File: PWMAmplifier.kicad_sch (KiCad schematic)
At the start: 13 parts, among them Q27 2N7000, Q28 2N7000, Q29 2N7000, Q30 2N7000, Q31 2N7000, Q32 2N7000

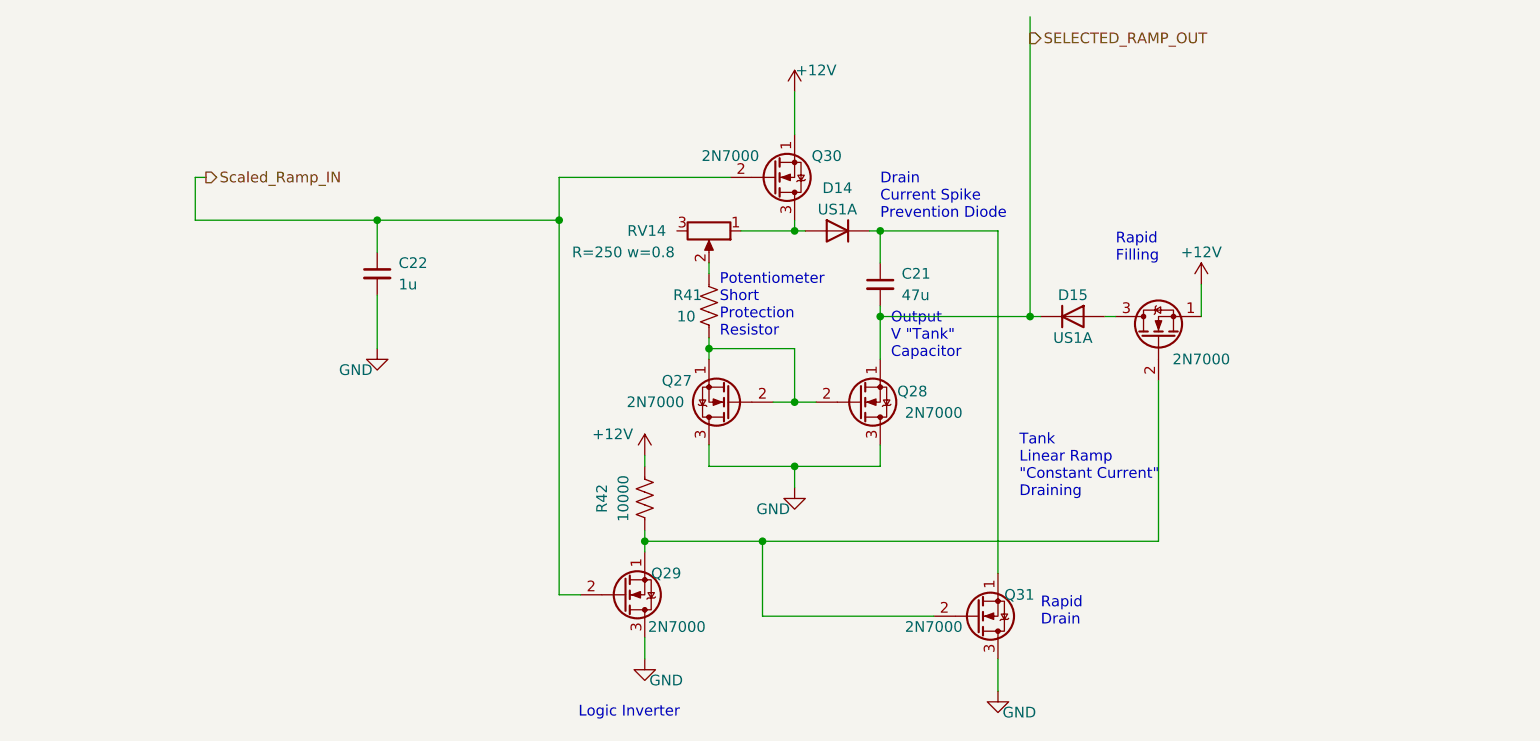
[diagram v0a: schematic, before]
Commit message: added new spice directives to improve simulation speed, added sections for motor drivers, micro controlers, i2c bus connections, realized that focusing coils, hv, horizontal and vertical ramp will need time stable signals (not voltage dependant like with a voltage controlled oscilator) so it will be much simpler to design them with micro controllers
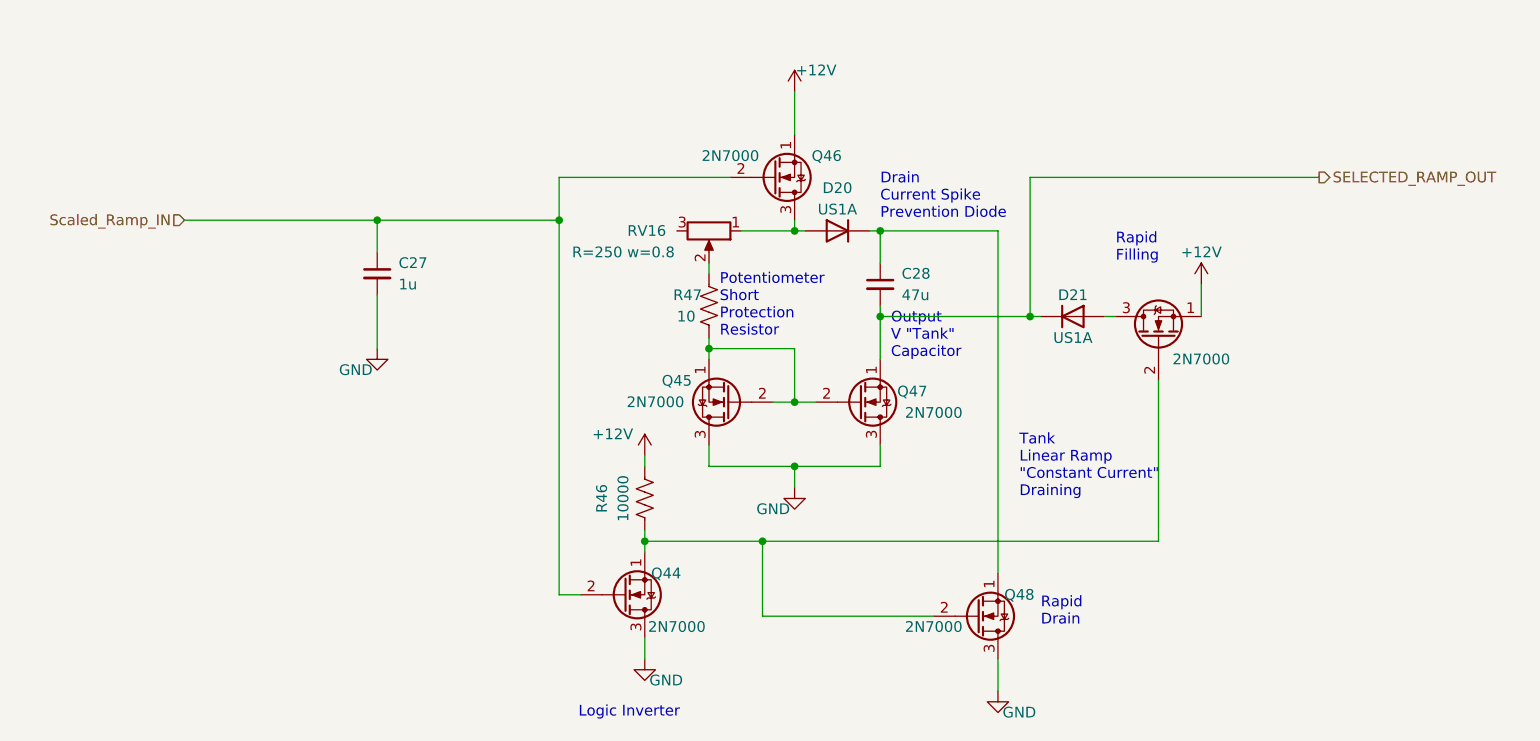
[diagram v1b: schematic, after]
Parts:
- renumbered C22 to C27, C21 to C28, D14 to D20, D15 to D21, Q29 to Q44, Q27 to Q45, Q30 to Q46, Q28 to Q47, Q31 to Q48, Q32 to Q49, R42 to R46, R41 to R47, RV14 to RV16
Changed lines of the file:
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@@
-	(wire
-		(pts
-			(xy 71.12 72.39) (xy 71.12 77.47)
-		)
-		(stroke
-			(width 0)
-			(type default)
-		)
-	)
-	(wire
-		(pts
-			(xy 71.12 77.47) (xy 92.71 77.47)
-		)
-		(stroke
-			(width 0)
-			(type default)
-		)
-	)
 	(wire
 		(pts
@@
 	(wire
 		(pts
-			(xy 170.18 53.34) (xy 170.18 88.9)
-		)
-		(stroke
-			(width 0)
-			(type default)
-		)
-	)
-	(wire
-		(pts
 			(xy 158.75 124.46) (xy 138.43 124.46)
 		)
@@
 	(wire
 		(pts
+			(xy 204.47 72.39) (xy 170.18 72.39)
+		)
+		(stroke
+			(width 0)
+			(type default)
+		)
+	)
+	(wire
+		(pts
 			(xy 152.4 78.74) (xy 151.13 78.74)
 		)
@@
 	(wire
 		(pts
-			(xy 72.39 72.39) (xy 71.12 72.39)
+			(xy 69.85 77.47) (xy 92.71 77.47)
 		)
 		(stroke
@@
 		(pts
 			(xy 124.46 127) (xy 124.46 129.54)
+		)
+		(stroke
+			(width 0)
+			(type default)
+		)
+	)
+	(wire
+		(pts
+			(xy 170.18 72.39) (xy 170.18 88.9)
 		)
 		(stroke
@@
 	(hierarchical_label "SELECTED_RAMP_OUT"
 		(shape output)
-		(at 170.18 55.88 0)
+		(at 204.47 72.39 0)
 		(fields_autoplaced yes)
 		(effects
@@
 	)
 	(hierarchical_label "Scaled_Ramp_IN"
-		(shape output)
-		(at 72.39 72.39 0)
+		(shape input)
+		(at 69.85 77.47 180)
 		(fields_autoplaced yes)
 		(effects
@@
 				(size 1.27 1.27)
 			)
-			(justify left)
+			(justify right)
 		)
 	)
@@
 		(on_board yes)
 		(dnp no)
-		(property "Reference" "D14"
+		(property "Reference" "D20"
 			(at 147.32 73.66 0)
 			(effects
@@
 		(on_board yes)
 		(dnp no)
-		(property "Reference" "RV14"
+		(property "Reference" "RV16"
 			(at 127 78.74 90)
 			(effects
@@
 		(on_board yes)
 		(dnp no)
-		(property "Reference" "Q30"
+		(property "Reference" "Q46"
 			(at 146.05 69.85 0)
 			(effects
@@
 		(on_board yes)
 		(dnp no)
-		(property "Reference" "#PWR089"
+		(property "Reference" "#PWR0112"
 			(at 166.37 139.7 0)
 			(effects
@@
 		(on_board yes)
 		(dnp no)
-		(property "Reference" "#PWR088"
+		(property "Reference" "#PWR0110"
 			(at 142.24 66.04 0)
 			(effects
@@
 		(on_board yes)
 		(dnp no)
-		(property "Reference" "#PWR090"
+		(property "Reference" "#PWR0113"
 			(at 190.5 88.9 0)
 			(effects
@@
 		(on_board yes)
 		(dnp no)
-		(property "Reference" "D15"
+		(property "Reference" "D21"
 			(at 175.26 86.36 0)
 			(effects
@@
 		(on_board yes)
 		(dnp no)
-		(property "Reference" "R42"
+		(property "Reference" "R46"
 			(at 119.38 110.49 90)
 			(effects
@@
 		(on_board yes)
 		(dnp no)
-		(property "Reference" "#PWR087"
+		(property "Reference" "#PWR0109"
 			(at 124.46 135.89 0)
 			(effects
@@
 		(on_board yes)
 		(dnp no)
-		(property "Reference" "#PWR081"
+		(property "Reference" "#PWR0108"
 			(at 124.46 109.22 0)
 			(effects
@@
 		(on_board yes)
 		(dnp no)
-		(property "Reference" "Q28"
+		(property "Reference" "Q47"
 			(at 156.21 97.79 0)
 			(effects
@@
 		(on_board yes)
 		(dnp no)
-		(property "Reference" "#PWR086"
+		(property "Reference" "#PWR0107"
 			(at 92.71 99.06 0)
 			(effects
@@
 		(on_board yes)
 		(dnp no)
-		(property "Reference" "Q29"
+		(property "Reference" "Q44"
 			(at 127 119.38 0)
 			(effects
@@
 		(on_board yes)
 		(dnp no)
-		(property "Reference" "#PWR085"
+		(property "Reference" "#PWR0111"
 			(at 142.24 115.57 0)
 			(effects
@@
 		(on_board yes)
 		(dnp no)
-		(property "Reference" "Q31"
+		(property "Reference" "Q48"
 			(at 168.91 121.92 0)
 			(effects
@@
 		(on_board yes)
 		(dnp no)
-		(property "Reference" "Q32"
+		(property "Reference" "Q49"
 			(at 185.42 85.09 90)
 			(effects
@@
 		(on_board yes)
 		(dnp no)
-		(property "Reference" "R41"
+		(property "Reference" "R47"
 			(at 129.54 86.36 0)
 			(effects
@@
 		(dnp no)
 		(fields_autoplaced yes)
-		(property "Reference" "C21"
+		(property "Reference" "C28"
 			(at 154.94 83.8263 0)
 			(effects
@@
 		(on_board yes)
 		(dnp no)
-		(property "Reference" "Q27"
+		(property "Reference" "Q45"
 			(at 128.27 96.52 0)
 			(effects
@@
 		(dnp no)
 		(fields_autoplaced yes)
-		(property "Reference" "C22"
+		(property "Reference" "C27"
 			(at 95.25 82.5563 0)
 			(effects
